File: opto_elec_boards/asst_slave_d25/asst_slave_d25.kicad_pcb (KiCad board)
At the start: 2 copper layers, 91.4 x 91.4 mm, 20 parts, among them J13 FromMainBoard, M4a MountingHole_4.3mm_M4, M4b MountingHole_4.3mm_M4, M4c MountingHole_4.3mm_M4, M4d MountingHole_4.3mm_M4, U1 TL082, U2 OPA551

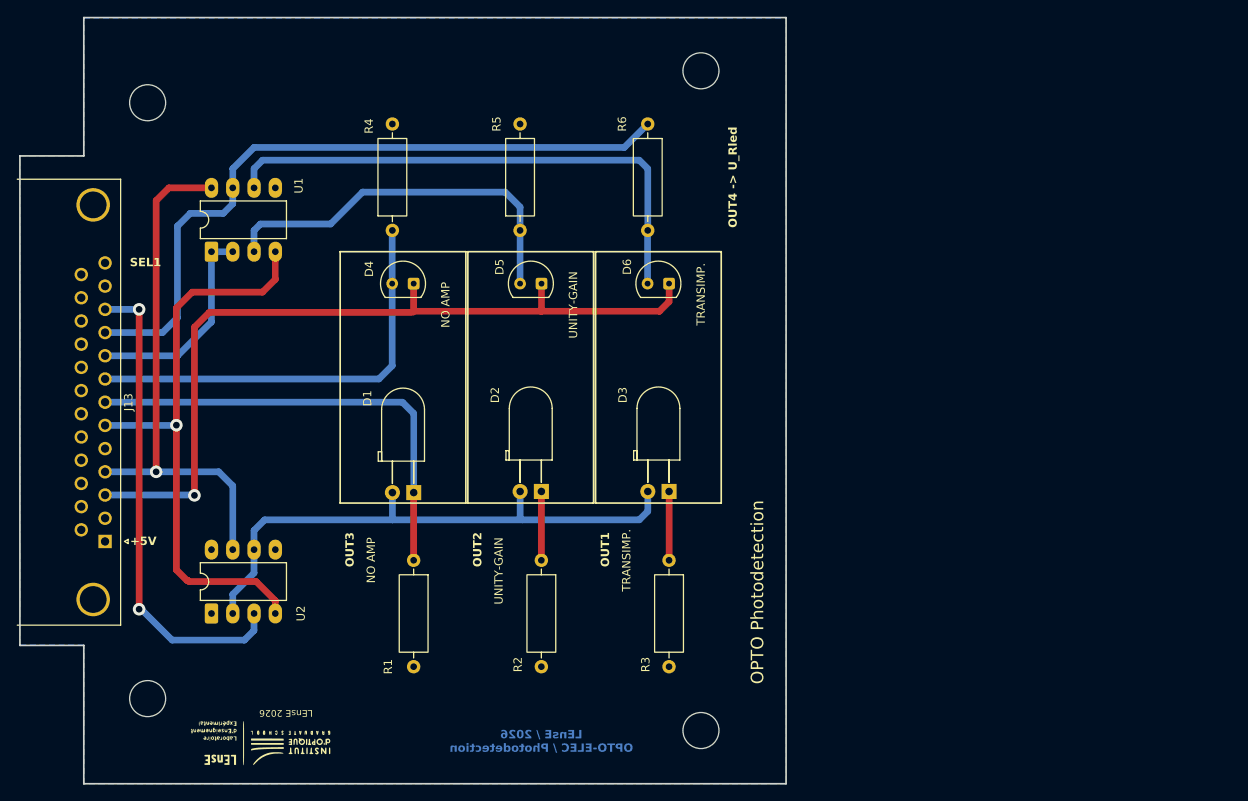
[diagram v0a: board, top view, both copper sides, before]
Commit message: Add Opto Board / Illuminance Control loop
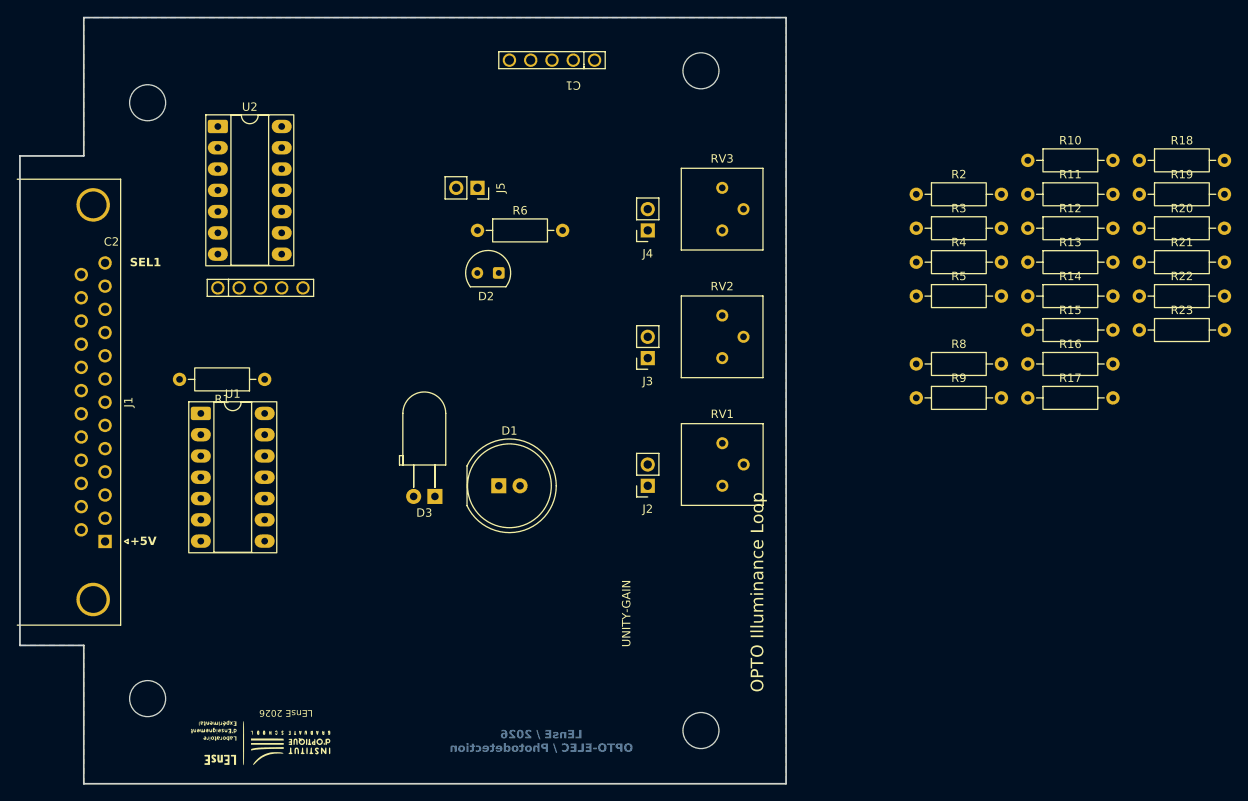
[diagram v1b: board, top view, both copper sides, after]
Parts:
- removed D4, D5, D6: SFH206K, LEnsE_devices:Osram_SFH206_2
- added C1: C, LEnsE_devices:C_R_Multi, F.Cu at (114.3, 40.6)
- added C2: C, LEnsE_devices:C_R_Multi, F.Cu at (74.4, 67.8)
- added J2: PID_Gain_OK, Connector_PinSocket_2.54mm:PinSocket_1x02_P2.54mm_Vertical, F.Cu at (123.2, 91.4)
- added J3: PID_Int_OK, Connector_PinSocket_2.54mm:PinSocket_1x02_P2.54mm_Vertical, F.Cu at (123.2, 76.2)
- added J4: PID_Der_OK, Connector_PinSocket_2.54mm:PinSocket_1x02_P2.54mm_Vertical, F.Cu at (123.2, 61.0)
- added J5: CLOSE, Connector_PinSocket_2.54mm:PinSocket_1x02_P2.54mm_Vertical, F.Cu at (102.9, 55.9)
- added R10: R, Resistor_THT:R_Axial_DIN0207_L6.3mm_D2.5mm_P10.16mm_Horizontal, F.Cu at (168.6, 52.6)
- added R11: R, Resistor_THT:R_Axial_DIN0207_L6.3mm_D2.5mm_P10.16mm_Horizontal, F.Cu at (168.6, 56.6)
- added R12: R, Resistor_THT:R_Axial_DIN0207_L6.3mm_D2.5mm_P10.16mm_Horizontal, F.Cu at (168.6, 60.7)
- added R13: R, Resistor_THT:R_Axial_DIN0207_L6.3mm_D2.5mm_P10.16mm_Horizontal, F.Cu at (168.6, 64.8)
- added R14: 12k, Resistor_THT:R_Axial_DIN0207_L6.3mm_D2.5mm_P10.16mm_Horizontal, F.Cu at (168.6, 68.8)
- added R15: 12k, Resistor_THT:R_Axial_DIN0207_L6.3mm_D2.5mm_P10.16mm_Horizontal, F.Cu at (168.6, 72.8)
- added R16: 12k, Resistor_THT:R_Axial_DIN0207_L6.3mm_D2.5mm_P10.16mm_Horizontal, F.Cu at (168.6, 76.9)
- added R17: R, Resistor_THT:R_Axial_DIN0207_L6.3mm_D2.5mm_P10.16mm_Horizontal, F.Cu at (168.6, 81.0)
- added R18: R, Resistor_THT:R_Axial_DIN0207_L6.3mm_D2.5mm_P10.16mm_Horizontal, F.Cu at (181.9, 52.6)
- added R19: R, Resistor_THT:R_Axial_DIN0207_L6.3mm_D2.5mm_P10.16mm_Horizontal, F.Cu at (181.9, 56.6)
- added R20: R, Resistor_THT:R_Axial_DIN0207_L6.3mm_D2.5mm_P10.16mm_Horizontal, F.Cu at (181.9, 60.7)
- added R21: 1k, Resistor_THT:R_Axial_DIN0207_L6.3mm_D2.5mm_P10.16mm_Horizontal, F.Cu at (181.9, 64.8)
- added R22: 490, Resistor_THT:R_Axial_DIN0207_L6.3mm_D2.5mm_P10.16mm_Horizontal, F.Cu at (181.9, 68.8)
- added R23: R, Resistor_THT:R_Axial_DIN0207_L6.3mm_D2.5mm_P10.16mm_Horizontal, F.Cu at (181.9, 72.8)
- added R8: R, Resistor_THT:R_Axial_DIN0207_L6.3mm_D2.5mm_P10.16mm_Horizontal, F.Cu at (155.2, 76.9)
- added R9: R, Resistor_THT:R_Axial_DIN0207_L6.3mm_D2.5mm_P10.16mm_Horizontal, F.Cu at (155.2, 81.0)
- added RV1: PID_Gain, Potentiometer_THT:Potentiometer_Bourns_3386P_Vertical, F.Cu at (132.1, 91.4)
- added RV2: PID_Integral, Potentiometer_THT:Potentiometer_Bourns_3386P_Vertical, F.Cu at (132.1, 76.2)
- added RV3: PID_Der, Potentiometer_THT:Potentiometer_Bourns_3386P_Vertical, F.Cu at (132.1, 61.0)
- D1: footprint LED_THT:LED_D5.0mm_Horizontal_O3.81mm_Z9.0mm -> LED_THT:LED_D10.0mm
- D2: value LED -> SFH206K; footprint LED_THT:LED_D5.0mm_Horizontal_O3.81mm_Z9.0mm -> LEnsE_devices:Osram_SFH206_2
- D3: value LED -> LED_Perturb
- R1, R2, R3: value 270 -> 47k; footprint Resistor_THT:R_Axial_DIN0309_L9.0mm_D3.2mm_P12.70mm_Horizontal -> Resistor_THT:R_Axial_DIN0207_L6.3mm_D2.5mm_P10.16mm_Horizontal
- R4: value 100k -> 47k; footprint Resistor_THT:R_Axial_DIN0309_L9.0mm_D3.2mm_P12.70mm_Horizontal -> Resistor_THT:R_Axial_DIN0207_L6.3mm_D2.5mm_P10.16mm_Horizontal
- R5: value 100k -> 270; footprint Resistor_THT:R_Axial_DIN0309_L9.0mm_D3.2mm_P12.70mm_Horizontal -> Resistor_THT:R_Axial_DIN0207_L6.3mm_D2.5mm_P10.16mm_Horizontal
- R6: footprint Resistor_THT:R_Axial_DIN0309_L9.0mm_D3.2mm_P12.70mm_Horizontal -> Resistor_THT:R_Axial_DIN0207_L6.3mm_D2.5mm_P10.16mm_Horizontal
- U1: value TL082 -> TL084; footprint Package_DIP:DIP-8_W7.62mm_LongPads -> Package_DIP:DIP-14_W7.62mm_Socket_LongPads
- U2: value OPA551 -> TL084; footprint Package_DIP:DIP-8_W7.62mm_LongPads -> Package_DIP:DIP-14_W7.62mm_Socket_LongPads
- moved R4 62.6 mm to (155.2, 64.8), turned to 0 degrees
- moved R2 62.5 mm to (155.2, 56.6), turned to 0 degrees
- moved U2 58.1 mm to (71.9, 48.6), turned to 0 degrees
- moved R3 49.4 mm to (155.2, 60.7), turned to 0 degrees
- moved R5 47.9 mm to (155.2, 68.8), turned to 0 degrees
- moved R1 28.0 mm to (77.5, 78.7), turned to 180 degrees
- moved D3 28.0 mm to (97.8, 92.7)
- moved D2 26.6 mm to (105.4, 66.0)
- moved R6 24.0 mm to (102.9, 61.0), turned to 0 degrees
- moved U1 19.3 mm to (69.8, 82.8), turned to 0 degrees
- moved D1 10.2 mm to (105.4, 91.4), turned to 0 degrees
- renumbered J13 to J1
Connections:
- D1 pad 1: OUT4 -> OUT2
- D2 pad 1: Net-(D2-K) -> RVAR_15V
- D2 pad 2: LED_IN -> MESURE
- D3 pad 1: Net-(D3-K) -> OUT4
- D3 pad 2: LED_IN -> IN_2
- J1 pad 10: OUT1 -> MESURE
- J1 pad 2: RVAR_5V -> Offset
- J1 pad 8: OUT3 -> ERREUR
- R1 pad 1: OUT4 -> PID_OUT
- R1 pad 2: GND -> Net-(U1A-+)
- R2 pad 1: Net-(D2-K) -> Offset
- R2 pad 2: GND -> Net-(U1A-+)
- R3 pad 1: Net-(D3-K) -> GND
- R3 pad 2: GND -> Net-(U1A--)
- R4 pad 1: OUT3 -> Net-(U1A--)
- R4 pad 2: GND -> LED_IN
- R5 pad 1: Net-(D5-A) -> OUT2
- R6 pad 1: OUT1 -> MESURE
- R6 pad 2: Net-(D6-A) -> GND
- U1 pad 1: OUT2 -> LED_IN
- U1 pad 2: OUT2 -> Net-(U1A--)
- U1 pad 3: Net-(D5-A) -> Net-(U1A-+)
- U1 pad 4: -15V -> +15V
- U1 pad 6: Net-(D6-A) -> Net-(U1B--)
- U1 pad 7: OUT1 -> Net-(J2-Pin_1)
- U1 pad 8: +15V -> Net-(R10-Pad1)
- U2 pad 1: unconnected-(U2-NULL-Pad1) -> Net-(J3-Pin_1)
- U2 pad 2: LED_IN -> Net-(U2A--)
- U2 pad 3: IN1 -> GND
- U2 pad 4: -15V -> +15V
- U2 pad 5: unconnected-(U2-NULL-Pad5) -> Net-(U2B-+)
- U2 pad 6: LED_IN -> Net-(U2B--)
- U2 pad 7: +15V -> ERREUR
- U2 pad 8: unconnected-(U2-NC-Pad8) -> Net-(J4-Pin_1)
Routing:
- net RVAR_15V: track 97.2 -> 0.00 mm, vias 1 -> 0
- net OUT1: track 83.9 -> 0.00 mm
- net -15V: track 71.2 -> 0.00 mm, vias 1 -> 0
- net LED_IN: track 68.0 -> 0.00 mm
- net Net-(D6-A): track 63.8 -> 0.00 mm
- net +15V: track 63.2 -> 0.00 mm, vias 1 -> 0
- net IN1: track 57.6 -> 0.00 mm, vias 2 -> 0
- net OUT4: track 54.9 -> 0.00 mm
- net OUT3: track 51.1 -> 0.00 mm
- net Net-(D5-A): track 46.1 -> 0.00 mm
- net OUT2: track 25.3 -> 0.00 mm
- net Net-(D2-K): track 8.22 -> 0.00 mm
- net Net-(D3-K): track 8.22 -> 0.00 mm
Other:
- board text added: "OPTO Illuminance Loop"
- board text removed: "NO AMP"
- board text removed: "OPTO Photodetection"
- board text removed: "OUT1"
- board text removed: "OUT2"
- board text removed: "OUT3"
- board text removed: "OUT4 -> U_Rled"
- board text removed: "TRANSIMP."

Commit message: Update Opto Board / Illuminance closed loop system
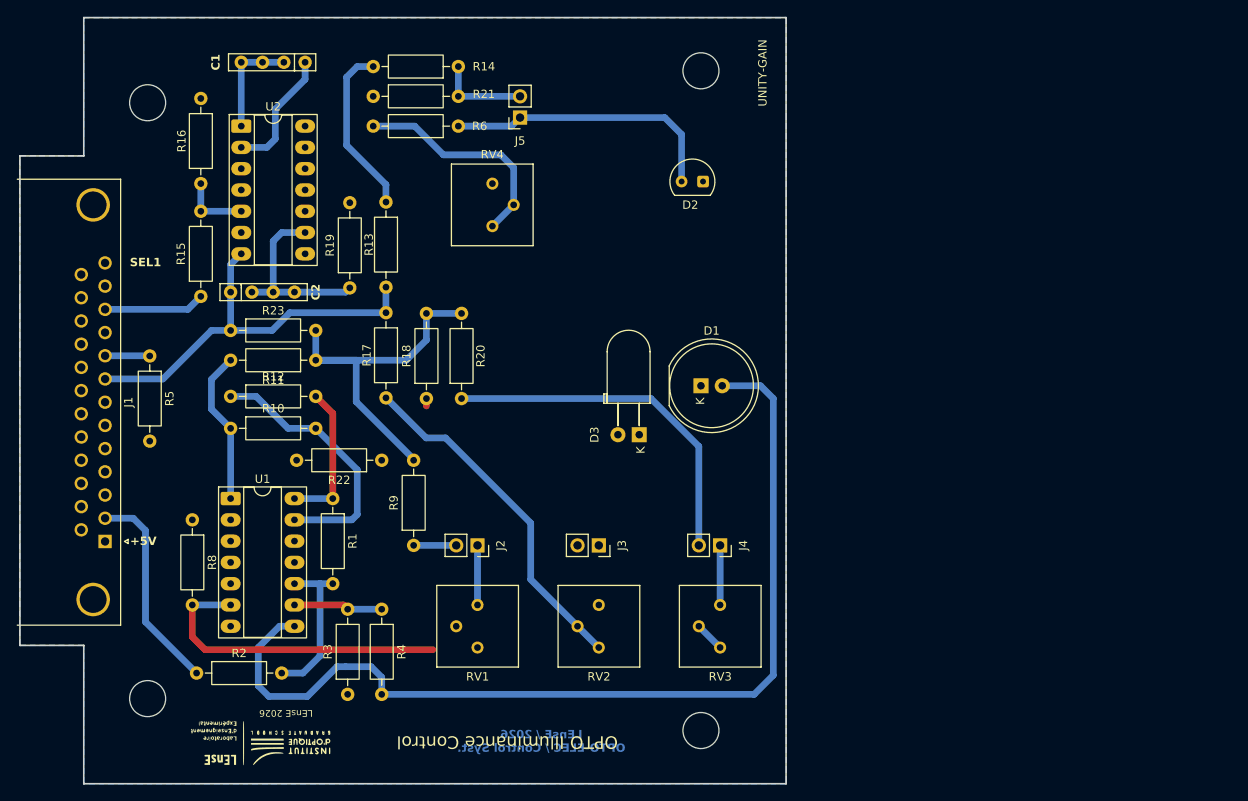
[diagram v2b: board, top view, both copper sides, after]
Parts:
- added RV4: Mesure_Gain, Potentiometer_THT:Potentiometer_Bourns_3386P_Vertical, F.Cu at (104.6, 60.5)
- R6: value 100k -> 10k
- moved R23 108.5 mm to (73.4, 72.9)
- moved R16 103.7 mm to (69.8, 45.2), turned to -90 degrees
- moved R2 103.2 mm to (69.3, 113.8)
- moved R10 100.4 mm to (73.4, 84.6)
- moved R15 98.8 mm to (69.8, 68.8), turned to 90 degrees
- moved R12 97.2 mm to (73.4, 80.8)
- moved R19 94.9 mm to (87.6, 67.8), turned to 90 degrees
- moved R21 93.6 mm to (90.4, 45.0)
- moved R22 92.5 mm to (91.4, 88.4), turned to 180 degrees
- moved R5 91.8 mm to (63.8, 75.9), turned to -90 degrees
- moved R18 89.7 mm to (96.8, 81.0), turned to 90 degrees
- moved R8 88.4 mm to (68.8, 95.5), turned to -90 degrees
- moved R3 87.8 mm to (87.4, 116.3), turned to 90 degrees
- moved R11 87.3 mm to (83.6, 76.5), turned to 180 degrees
- moved R20 83.4 mm to (101.0, 81.0), turned to 90 degrees
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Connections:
- D3 pad 2: IN_2 -> IN2
- R1 pad 2: Net-(U1A-+) -> Net-(U1C-+)
- R11 pad 1: Net-(U1C--) -> Net-(U1A--)
- R15 pad 1: IN_1 -> IN1
- R18 pad 2: Net-(U1C--) -> Net-(U1A--)
- R2 pad 2: Net-(U1A-+) -> Net-(U1C-+)
- R20 pad 2: Net-(U1C--) -> Net-(U1A--)
- R23 pad 2: Net-(U1C--) -> Net-(U1A--)
- R3 pad 2: Net-(U1A--) -> Net-(U1C--)
- R4 pad 1: Net-(U1A--) -> Net-(U1C--)
- R6 pad 2: GND -> Net-(R6-Pad2)
- R9 pad 2: Net-(U1C--) -> Net-(U1A--)
- U1 pad 1: LED_IN -> Net-(R10-Pad1)
- U1 pad 10: GND -> Net-(U1C-+)
- U1 pad 3: Net-(U1A-+) -> GND
- U1 pad 8: Net-(R10-Pad1) -> LED_IN
- U2 pad 10: unconnected-(U2C-+-Pad10) -> GND
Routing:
- net LED_IN: track 0.00 -> 116.7 mm
- net ERREUR: track 0.00 -> 49.5 mm
- net Net-(U1A--): track 0.00 -> 44.7 mm
- net Net-(J4-Pin_2): track 0.00 -> 42.5 mm
- net Net-(R17-Pad2): track 0.00 -> 41.7 mm
- net Net-(U1B--): track 0.00 -> 37.7 mm
- net MESURE: track 0.00 -> 33.5 mm
- net Net-(U1D--): track 0.00 -> 31.8 mm
- net Net-(R6-Pad2): track 0.00 -> 26.9 mm
- net Offset: track 0.00 -> 25.0 mm
- net Net-(U2C--): track 0.00 -> 22.2 mm
- net Net-(U2B--): track 0.00 -> 20.5 mm
- net Net-(U1C-+): track 0.00 -> 18.6 mm
- net Net-(R10-Pad1): track 0.00 -> 18.4 mm
- net PID_OUT: track 0.00 -> 17.6 mm
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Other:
- board text added: "K"
- board text added: "LEnsE / 2026 OPTO-ELEC / Control Syst."
- board text added: "OPTO Illuminance Control"
- board text removed: "LEnsE / 2026 OPTO-ELEC / Photodetection"
- board text removed: "OPTO Illuminance Loop"

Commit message: Update Opto Board / Update Illuminance Control - analog circuit PID
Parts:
- removed R11: R, Resistor_THT:R_Axial_DIN0207_L6.3mm_D2.5mm_P10.16mm_Horizontal
- moved R6 14.3 mm to (97.0, 62.4), turned to 90 degrees
- moved R9 6.35 mm to (100.3, 94.7), turned to 180 degrees
- moved R21 3.57 mm to (90.7, 48.5)
- moved R14 3.57 mm to (100.8, 45.0)
- moved R8 1.02 mm to (67.8, 95.5)
- moved R15 1.02 mm to (68.8, 68.8)
- moved C2 0.63 mm to (75.9, 67.7)
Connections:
- D2 pad 1: RVAR_15V -> +15V
- D2 pad 2: MESURE -> Net-(D2-A)
- R18 pad 2: Net-(U1A--) -> Net-(U1D--)
- R20 pad 2: Net-(U1A--) -> Net-(U1D--)
- R23 pad 2: Net-(U1A--) -> Net-(U1D--)
- R6 pad 1: MESURE -> Net-(D2-A)
- R9 pad 2: Net-(U1A--) -> Net-(U1D--)
- U1 pad 1: Net-(R10-Pad1) -> (no net)
- U1 pad 2: Net-(U1A--) -> (no net)
- U1 pad 3: GND -> (no net)
- U2 pad 12: unconnected-(U2D-+-Pad12) -> Net-(D2-A)
- U2 pad 13: unconnected-(U2D---Pad13) -> MESURE
- U2 pad 14: unconnected-(U2-Pad14) -> MESURE
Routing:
- net +15V: track 0.00 -> 227.2 mm, vias 0 -> 1
- net IN2: track 0.00 -> 137.7 mm, vias 0 -> 1
- net Net-(U2A--): track 15.1 -> 122.0 mm, vias 0 -> 1
- net Net-(J3-Pin_1): track 12.7 -> 108.1 mm, vias 0 -> 1
- net Net-(R19-Pad2): track 3.59 -> 88.1 mm
- net OUT4: track 0.00 -> 81.0 mm
- net OUT2: track 5.34 -> 83.2 mm, vias 0 -> 2
- net -15V: track 0.00 -> 73.3 mm, vias 0 -> 1
- net Net-(J4-Pin_1): track 7.11 -> 76.4 mm
- net Net-(D2-A): track 0.00 -> 59.7 mm
- net MESURE: track 33.5 -> 87.3 mm
- net Net-(U1A--): track 44.7 -> 0.00 mm
- net Net-(U1D--): track 31.8 -> 67.8 mm
- net Net-(J2-Pin_1): track 7.11 -> 39.3 mm
- net Net-(U2B--): track 20.5 -> 45.6 mm, vias 0 -> 1
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
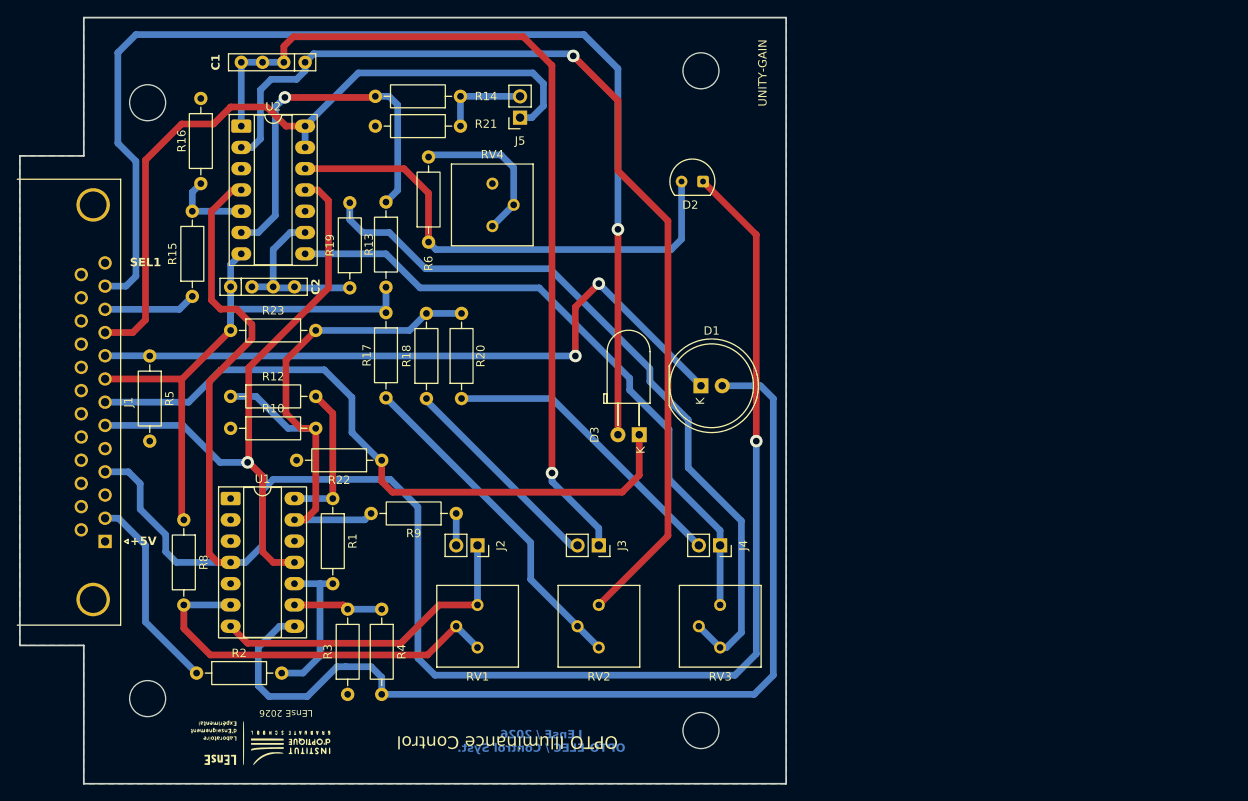
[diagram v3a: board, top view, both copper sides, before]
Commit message: Update Opto Boards / Finish Illuminance Control Syst.
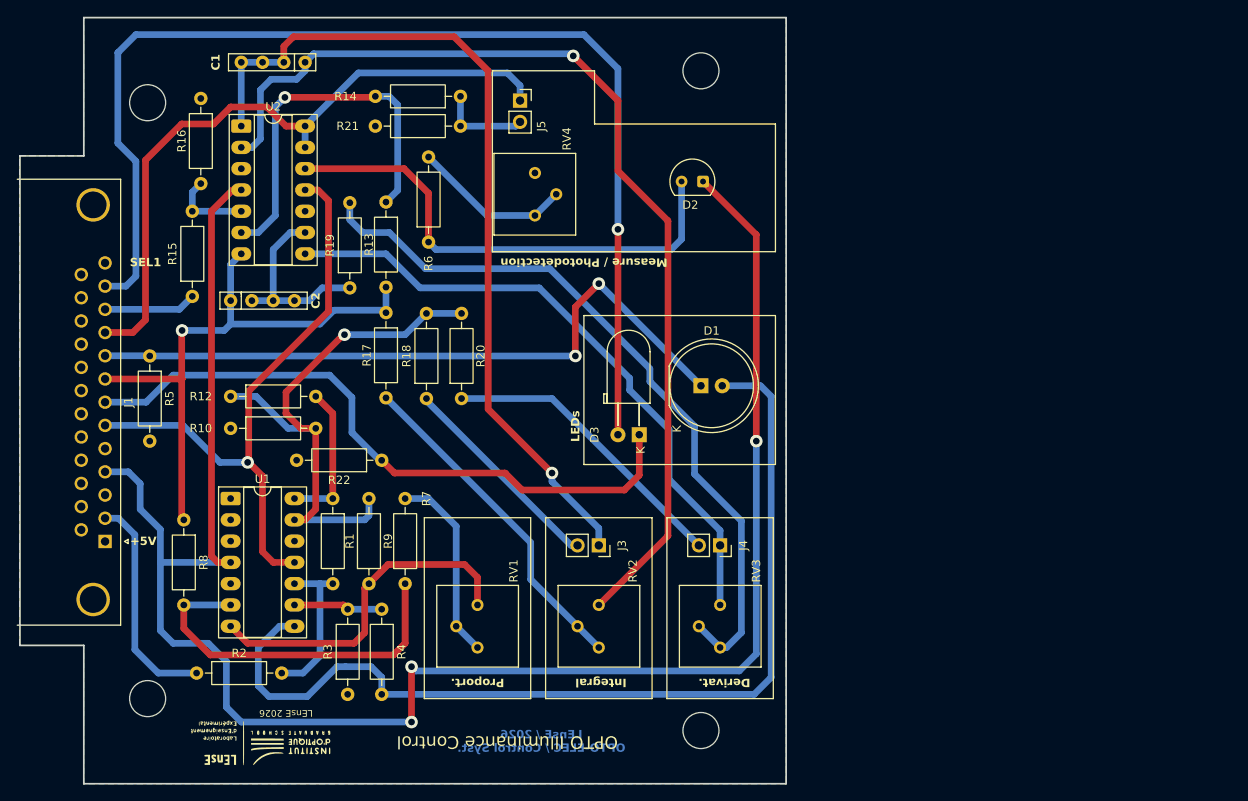
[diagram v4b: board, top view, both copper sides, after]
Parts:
- removed J2: PID_Gain_OK, Connector_PinSocket_2.54mm:PinSocket_1x02_P2.54mm_Vertical
- removed R23: R, Resistor_THT:R_Axial_DIN0207_L6.3mm_D2.5mm_P10.16mm_Horizontal
- added R7: R, Resistor_THT:R_Axial_DIN0207_L6.3mm_D2.5mm_P10.16mm_Horizontal, F.Cu at (94.2, 103.1)
- moved R9 13.4 mm to (89.9, 103.1), turned to 90 degrees
- moved RV4 5.24 mm to (109.7, 59.2)
- moved J5 2.03 mm to (108.0, 45.5), turned to 0 degrees
- moved C2 1.65 mm to (75.9, 69.3)
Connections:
- RV1 pad 1: Net-(J2-Pin_1) -> PID_Gain_OUT
- RV1 pad 2: Net-(U1B--) -> Net-(R7-Pad2)
- RV1 pad 3: Net-(U1B--) -> Net-(R7-Pad2)
- U1 pad 7: Net-(J2-Pin_1) -> PID_Gain_OUT
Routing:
- net Net-(J2-Pin_1): track 39.3 -> 0.00 mm
- net PID_Gain_OUT: track 3.81 -> 41.3 mm
- net Net-(R7-Pad2): track 0.00 -> 23.0 mm
- net MESURE: track 87.3 -> 80.4 mm
- net Net-(J3-Pin_1): track 108.1 -> 103.3 mm
- net Net-(U1B--): track 47.2 -> 43.8 mm
- net Offset: track 23.9 -> 26.6 mm
- net OUT4: track 81.0 -> 78.8 mm
- net Net-(U2C--): track 20.9 -> 23.1 mm
- net +15V: track 227.2 -> 225.6 mm, vias 1 -> 3
- net ERREUR: track 68.3 -> 69.4 mm, vias 0 -> 1
- net Net-(U1D--): track 67.8 -> 67.3 mm, vias 0 -> 1
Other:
- board text added: "Derivat."
- board text added: "Integral"
- board text added: "LEDs"
- board text added: "Measure / Photodetection"
- board text added: "Proport."
- board text removed: "UNITY-GAIN"
